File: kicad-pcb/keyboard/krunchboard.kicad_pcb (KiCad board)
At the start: 2 copper layers, 427.6 x 139.1 mm, 212 parts, among them J1 Conn_01x04_Pin, J2 Conn_01x04_Pin, SW1 SW_Push_45deg, SW10 SW_Push_45deg, SW11 SW_Push_45deg, SW12 SW_Push_45deg, SW13 SW_Push_45deg, SW14 SW_Push_45deg, SW15 SW_Push_45deg, SW16 SW_Push_45deg, SW17 SW_Push_45deg, SW18 SW_Push_45deg, SW19 SW_Push_45deg, SW2 SW_Push_45deg, SW20 SW_Push_45deg, SW21 SW_Push_45deg, SW22 SW_Push_45deg, SW23 SW_Push_45deg, SW24 SW_Push_45deg, SW25 SW_Push_45deg, SW26 SW_Push_45deg, SW27 SW_Push_45deg, SW28 SW_Push_45deg, SW29 SW_Push_45deg, SW3 SW_Push_45deg, SW30 SW_Push_45deg, SW31 SW_Push_45deg, SW32 SW_Push_45deg, SW33 SW_Push_45deg, SW34 SW_Push_45deg, SW35 SW_Push_45deg, SW36 SW_Push_45deg, SW37 SW_Push_45deg, SW38 SW_Push_45deg, SW39 SW_Push_45deg, SW4 SW_Push_45deg, SW40 SW_Push_45deg, SW41 SW_Push_45deg, SW42 SW_Push_45deg, SW43 SW_Push_45deg, SW44 SW_Push_45deg, SW45 SW_Push_45deg, SW46 SW_Push_45deg, SW47 SW_Push_45deg, SW48 SW_Push_45deg, SW49 SW_Push_45deg, SW5 SW_Push_45deg, SW50 SW_Push_45deg, SW51 SW_Push_45deg, SW52 SW_Push_45deg, SW53 SW_Push_45deg, SW54 SW_Push_45deg, SW55 SW_Push_45deg, SW56 SW_Push_45deg, SW57 SW_Push_45deg, SW58 SW_Push_45deg, SW59 SW_Push_45deg, SW6 SW_Push_45deg, SW60 SW_Push_45deg, SW61 SW_Push_45deg, SW62 SW_Push_45deg, SW63 SW_Push_45deg, SW64 SW_Push_45deg, SW65 SW_Push_45deg, SW66 SW_Push_45deg, SW67 SW_Push_45deg, SW68 SW_Push_45deg, SW69 SW_Push_45deg, SW7 SW_Push_45deg, SW70 SW_Push_45deg, SW71 SW_Push_45deg, SW72 SW_Push_45deg, SW73 SW_Push_45deg, SW74 SW_Push_45deg, SW75 SW_Push_45deg, SW76 SW_Push_45deg, SW77 SW_Push_45deg, SW78 SW_Push_45deg, SW79 SW_Push_45deg, SW8 SW_Push_45deg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

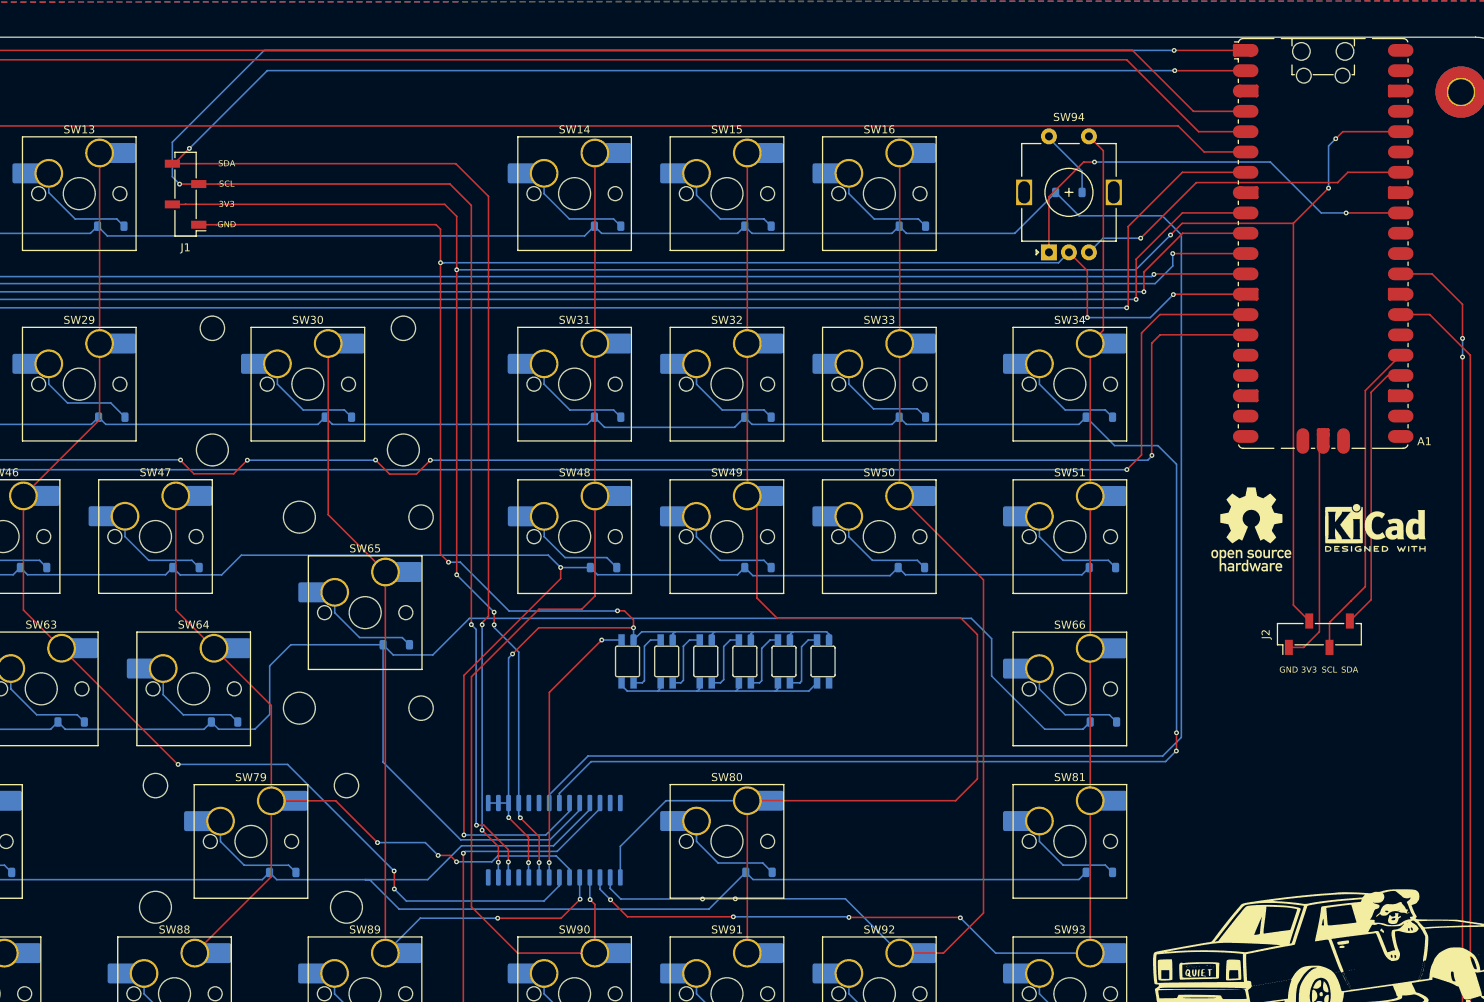
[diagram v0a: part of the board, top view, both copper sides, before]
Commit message: updated pcb - switched oled socket from smd to tht, added hole for tht socket in case, adjusted pcb vias and silkscreen, added testpoints to pcb
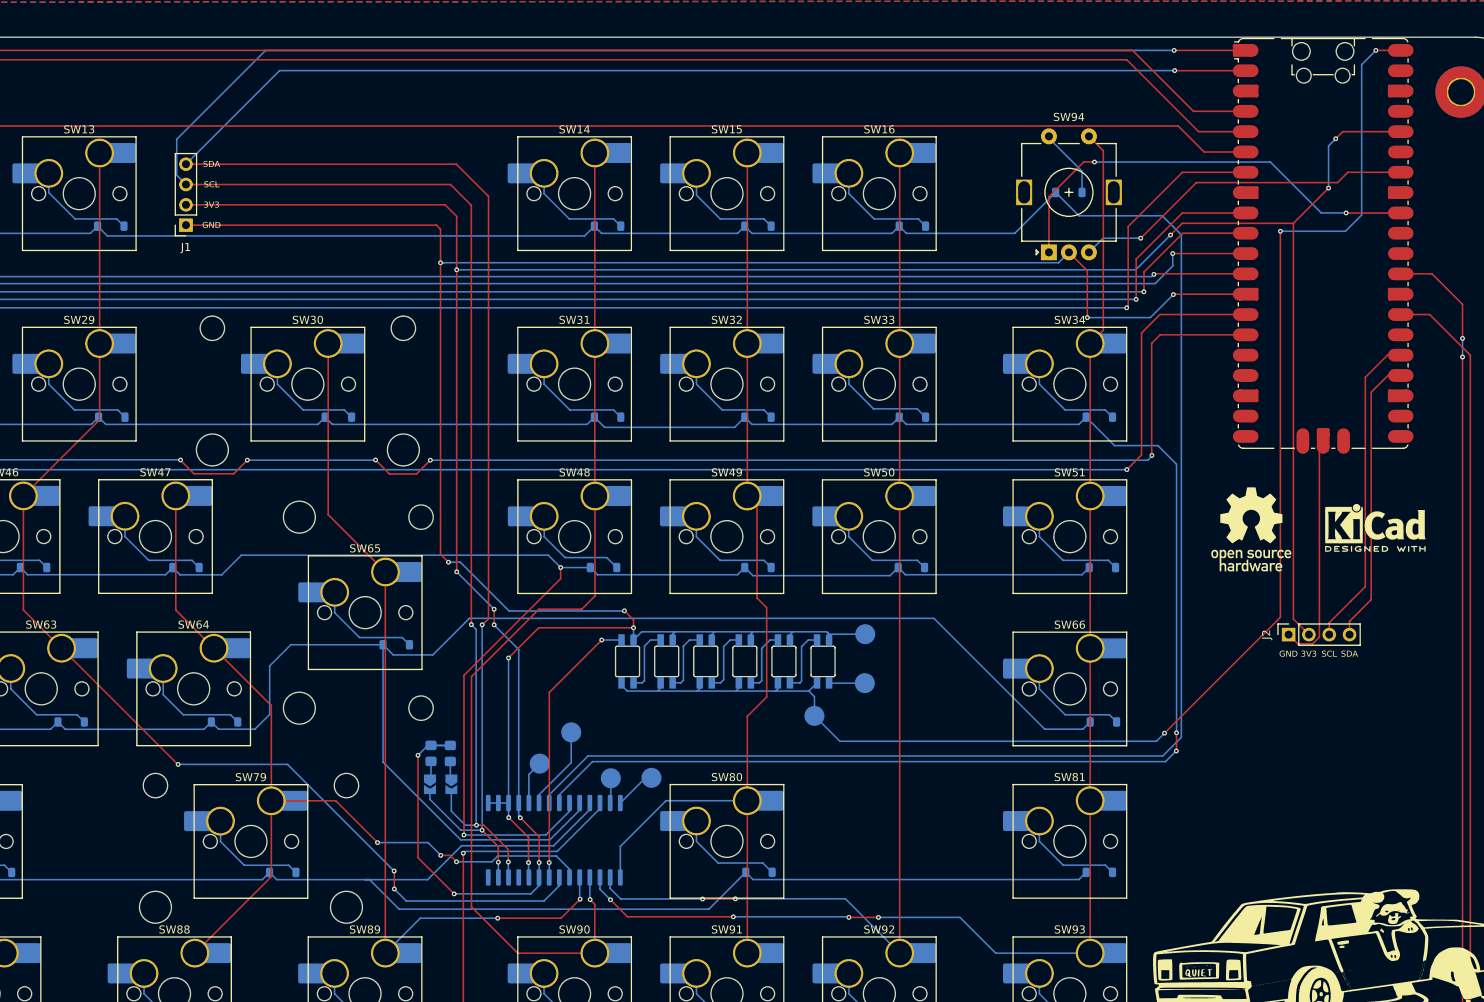
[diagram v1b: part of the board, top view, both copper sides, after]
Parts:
- added 5V1: TestPoint, TestPoint:TestPoint_Pad_D2.5mm, B.Cu at (418.5, 167.3)
- added GND1: TestPoint, TestPoint:TestPoint_Pad_D2.5mm, B.Cu at (424.9, 157.0)
- added GPA6: TestPoint, TestPoint:TestPoint_Pad_D2.5mm, B.Cu at (393.1, 175.1)
- added GPA7: TestPoint, TestPoint:TestPoint_Pad_D2.5mm, B.Cu at (398.1, 175.0)
- added JP1: SolderJumper_2_Open, Jumper:SolderJumper-2_P1.3mm_Open_TrianglePad1.0x1.5mm, B.Cu at (370.5, 175.8)
- added JP2: SolderJumper_2_Open, Jumper:SolderJumper-2_P1.3mm_Open_TrianglePad1.0x1.5mm, B.Cu at (373.1, 175.8)
- added MCP_INTA1: TestPoint, TestPoint:TestPoint_Pad_D2.5mm, B.Cu at (388.1, 169.3)
- added MCP_INTB1: TestPoint, TestPoint:TestPoint_Pad_D2.5mm, B.Cu at (384.2, 173.2)
- added NEOPIXEL_DOUT1: TestPoint, TestPoint:TestPoint_Pad_D2.5mm, B.Cu at (424.8, 163.2)
- added R1: R4.7k, Resistor_SMD:R_0805_2012Metric_Pad1.20x1.40mm_HandSolder, B.Cu at (370.6, 171.9)
- added R2: R4.7k, Resistor_SMD:R_0805_2012Metric_Pad1.20x1.40mm_HandSolder, B.Cu at (373.0, 172.0)
- J1, J2: footprint Connector_PinSocket_2.54mm:PinSocket_1x04_P2.54mm_Vertical_SMD_Pin1Left -> Connector_PinSocket_2.54mm:PinSocket_1x04_P2.54mm_Vertical
- moved J1 3.87 mm to (340.0, 105.9)
- moved J2 3.85 mm to (477.8, 157.1)
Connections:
- A1 pad 40: unconnected-(A1-VBUS-Pad40) -> +5V
- D95 pad 2: unconnected-(D95-DOUT-Pad2) -> Net-(D95-DOUT)
- U1 pad 19: unconnected-(U1-INTB-Pad19) -> Net-(U1-INTB)
- U1 pad 20: unconnected-(U1-INTA-Pad20) -> Net-(U1-INTA)
- U1 pad 27: unconnected-(U1-GPA6-Pad27) -> Net-(U1-GPA6)
- U1 pad 28: unconnected-(U1-GPA7-Pad28) -> Net-(U1-GPA7)
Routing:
- net +5V: track 30.1 -> 183.2 mm, vias 0 -> 3
- net C16: track 174.7 -> 124.1 mm
- net +3V3: track 301.8 -> 340.0 mm, vias 9 -> 11
- net C17: track 152.8 -> 141.0 mm
- net Net-(U1-INTA): track 0.00 -> 10.5 mm
- net GND: track 318.4 -> 325.5 mm
- net SDA0: track 266.5 -> 272.4 mm, vias 5 -> 4
- net SCL0: track 268.6 -> 274.1 mm, vias 5 -> 4
- net Net-(U1-INTB): track 0.00 -> 5.49 mm
- net Net-(U1-GPA7): track 0.00 -> 5.20 mm
- net Net-(D95-DOUT): track 0.00 -> 4.49 mm
- net Net-(U1-GPA6): track 0.00 -> 3.13 mm
- net R3: track 419.8 -> 417.1 mm
- net Net-(JP1-A): track 0.00 -> 2.19 mm
- net Net-(JP2-A): track 0.00 -> 2.17 mm
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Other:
- board text added: "5V"
- board text added: "DOUT"
- board text added: "INTA"
- board text added: "INTB"
- board text added: "MCP23017 SOIC-28"

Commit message: final v1 pcb revision, plate update
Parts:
- added G***: LOGO, LOGO, B.Cu at (350.5, 101.6)
- added logo1: KiCad-Logo2_5mm_SilkScreen, Symbol:KiCad-Logo2_5mm_SilkScreen, B.Cu at (367.0, 101.6)
- moved G*** 18.4 mm to (491.5, 144.0)
- moved logo1 13.6 mm to (475.0, 144.0)
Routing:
- net SDA0: track 272.4 -> 237.8 mm, vias 4 -> 3
- net C1: track 625.1 -> 619.0 mm
- net +5V: track 183.2 -> 178.4 mm
- net C4: track 389.3 -> 393.4 mm, vias 0 -> 1
- net GND: track 325.5 -> 321.7 mm
- net SCL0: track 274.1 -> 270.7 mm, vias 4 -> 3
- net C0: track 621.3 -> 618.2 mm
- net C2: track 461.1 -> 458.3 mm, vias 0 -> 1
- net C3: track 438.1 -> 435.8 mm, vias 0 -> 1
- net C15: track 131.3 -> 129.8 mm
- net C11: track 295.9 -> 295.0 mm
- net C10: track 315.5 -> 314.6 mm
- net C13: track 108.5 -> 107.9 mm
